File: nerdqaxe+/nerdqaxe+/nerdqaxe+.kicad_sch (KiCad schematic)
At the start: 4 parts, among them J3 Barrel_Jack_Switch

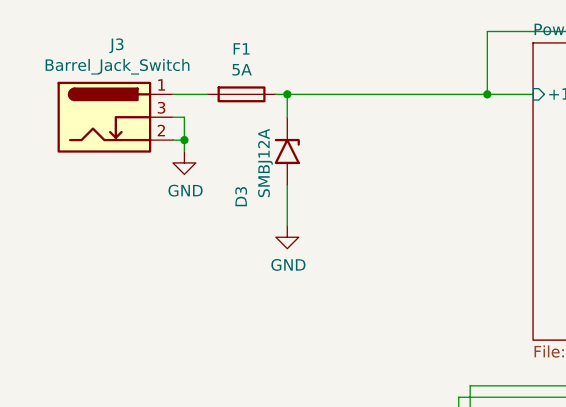
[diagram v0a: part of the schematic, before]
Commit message: updated bom of + for 24V cap
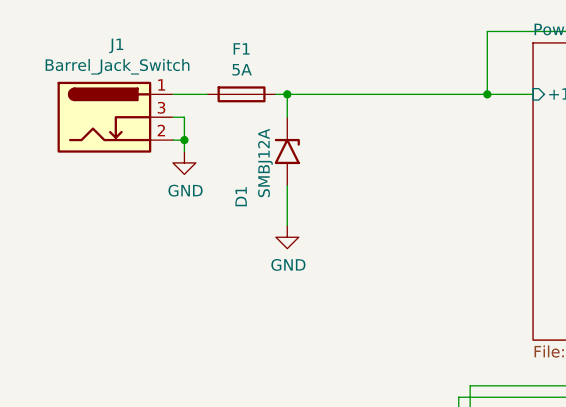
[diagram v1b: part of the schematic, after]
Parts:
- renumbered D3 to D1, J3 to J1
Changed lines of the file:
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@@
 (kicad_sch
-	(version 20231120)
+	(version 20250114)
 	(generator "eeschema")
-	(generator_version "8.0")
+	(generator_version "9.0")
 	(paper "A")
 	(title_block
@@
 		(on_board yes)
 		(dnp no)
-		(property "Reference" "#PWR012"
+		(property "Reference" "#PWR04"
 			(at 55.245 73.025 0)
 			(effects
@@
 		(on_board yes)
 		(dnp no)
-		(property "Reference" "J3"
+		(property "Reference" "J1"
 			(at 36.3728 46.5582 0)
 			(effects
@@
 		(on_board yes)
 		(dnp no)
-		(property "Reference" "D3"
+		(property "Reference" "D1"
 			(at 50.165 62.23 0)
 			(effects
@@
 		(on_board yes)
 		(dnp no)
-		(property "Reference" "#PWR01"
+		(property "Reference" "#PWR03"
 			(at 43.815 64.77 0)
 			(effects
@@
 		(at 82.55 91.44)
 		(size 17.78 26.67)
+		(exclude_from_sim no)
+		(in_bom yes)
+		(on_board yes)
+		(dnp no)
 		(fields_autoplaced yes)
 		(stroke
@@
 		(at 82.55 46.355)
 		(size 17.145 33.02)
+		(exclude_from_sim no)
+		(in_bom yes)
+		(on_board yes)
+		(dnp no)
 		(fields_autoplaced yes)
 		(stroke
@@
 		(at 144.78 83.82)
 		(size 39.37 29.845)
+		(exclude_from_sim no)
+		(in_bom yes)
+		(on_board yes)
+		(dnp no)
 		(fields_autoplaced yes)
 		(stroke
@@
 		)
 	)
+	(embedded_fonts no)
 )
